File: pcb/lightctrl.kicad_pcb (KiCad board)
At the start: 2 copper layers, 71.1 x 22.9 mm, 30 parts, among them IC1 ESP-WROOM-02, P1 LED_CONN, P2 PROG, P3 IO, P4 BATT_SENSE, P5 5V, Q1 BSS138, Q2 IRF8788, SW1 SW_FLASH, SW2 SW_RST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

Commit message: Fixed bottom silkscreen text
Moved text away from pin headers
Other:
- board text added: "github.com/polygon/lightctrl"
- board text removed: "https://github.com/polygon/lightctrl"
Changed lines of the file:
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@@
     (links 73)
     (no_connects 0)
-    (area 77.419999 49.479999 148.640001 72.440001)
+    (area 71.511399 48.101 149.017334 73.886924)
     (thickness 1.6002)
     (drawings 34)
@@
   (page A4)
   (layers
-    (0 F.Cu signal)
-    (31 B.Cu signal)
+    (0 F.Cu signal hide)
+    (31 B.Cu signal hide)
     (36 B.SilkS user)
-    (37 F.SilkS user)
+    (37 F.SilkS user hide)
     (38 B.Mask user)
     (39 F.Mask user)
@@
     (effects (font (size 1 1) (thickness 0.15)))
   )
-  (gr_text https://github.com/polygon/lightctrl (at 78.1685 70.2945) (layer B.SilkS)
-    (effects (font (size 1.5 1.5) (thickness 0.3)) (justify right mirror))
-  )
-  (gr_text "Wi-Fi LED Controller\njan@legxaro.de\nchris@priseko.de" (at 147.32 67.945) (layer B.SilkS)
+  (gr_text github.com/polygon/lightctrl (at 78.232 67.056) (layer B.SilkS)
+    (effects (font (size 1.35 1.35) (thickness 0.3)) (justify right mirror))
+  )
+  (gr_text "Wi-Fi LED Controller\njan@legxaro.de\nchris@priseko.de" (at 144.399 64.77) (layer B.SilkS)
     (effects (font (size 1.5 1.5) (thickness 0.3)) (justify left mirror))
   )
-  (gr_text <<</>> (at 122.809 55.626) (layer B.SilkS)
-    (effects (font (size 7 7) (thickness 1.75)) (justify mirror))
+  (gr_text <<</>> (at 100.711 57.912) (layer B.SilkS)
+    (effects (font (size 6 6) (thickness 1.5)) (justify mirror))
   )
   (gr_text IO (at 108.458 67.564) (layer F.SilkS)

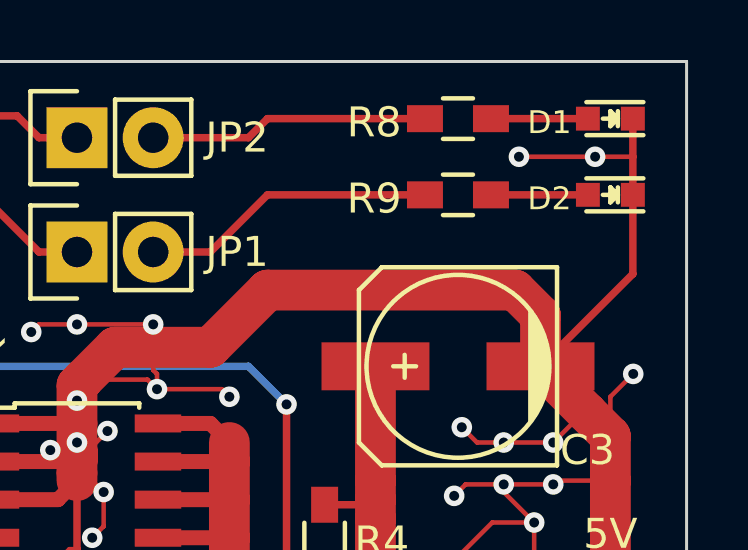
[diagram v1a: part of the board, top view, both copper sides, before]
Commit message: Replaced LED footprint with 3.2mmx1.6mm
Reasonable LED part available with that footprint
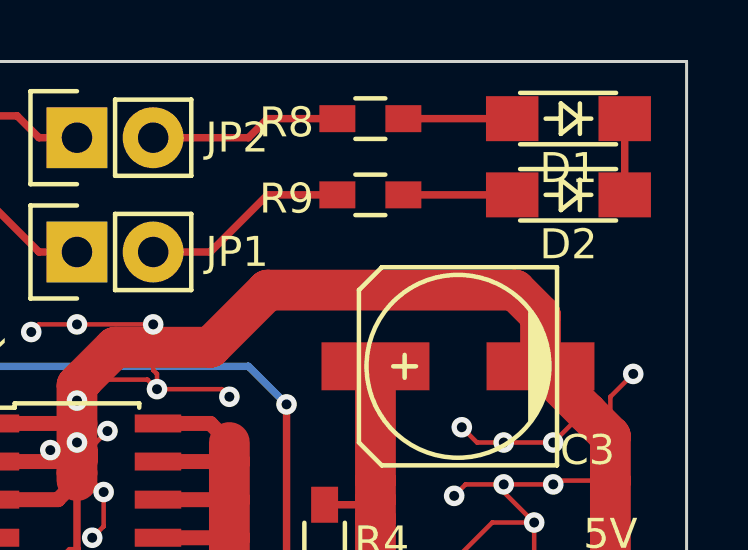
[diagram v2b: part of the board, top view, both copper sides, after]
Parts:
- D1, D2: footprint LEDs:LED_0603 -> leds:LED_3.2x1.6
- moved R8 2.92 mm to (138.0, 51.4)
- moved R9 2.92 mm to (138.0, 54.0)
- moved D1 1.40 mm to (144.7, 51.4)
- moved D2 1.40 mm to (144.7, 54.0)
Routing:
- net GND: track 123.7 -> 112.9 mm, vias 28 -> 26
- net Net-(JP2-Pad2): track 9.32 -> 6.40 mm
- net Net-(JP1-Pad2): track 9.85 -> 6.93 mm

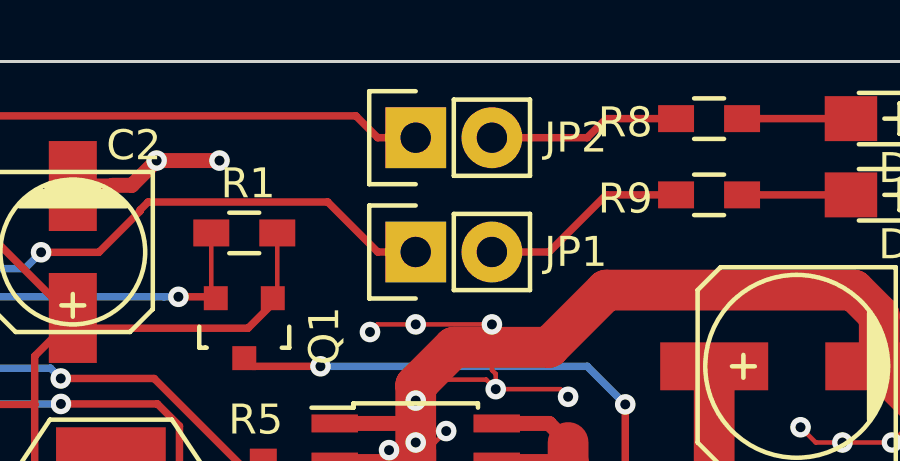
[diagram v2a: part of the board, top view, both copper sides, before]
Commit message: Routing and silkscreen fixes
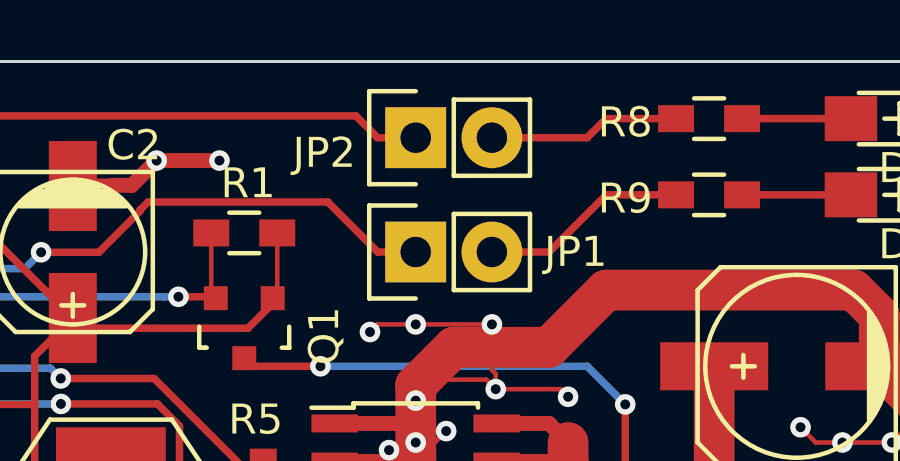
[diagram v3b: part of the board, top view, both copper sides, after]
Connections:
- IC1 pad 11: /ESP8266/RXI -> /ESP8266/TXO
- IC1 pad 12: /ESP8266/TXO -> /ESP8266/RXI
- P2 pad 2: /ESP8266/RXI -> /ESP8266/TXO
- P2 pad 3: /ESP8266/TXO -> /ESP8266/RXI
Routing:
- net /ESP8266/TXO: track 18.0 -> 20.2 mm
- net /ESP8266/RXI: track 20.2 -> 18.0 mm
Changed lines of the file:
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@@
   )
   (setup
-    (last_trace_width 0.25)
+    (last_trace_width 0.1524)
     (user_trace_width 0.25)
     (user_trace_width 0.5)
@@
       (net 13 /ESP8266/BOOT_SEL))
     (pad 11 smd oval (at 18 10.5 90) (size 2 0.9) (layers F.Cu F.Mask)
+      (net 15 /ESP8266/TXO))
+    (pad 12 smd oval (at 18 9 90) (size 2 0.9) (layers F.Cu F.Mask)
       (net 14 /ESP8266/RXI))
-    (pad 12 smd oval (at 18 9 90) (size 2 0.9) (layers F.Cu F.Mask)
-      (net 15 /ESP8266/TXO))
     (pad 13 smd oval (at 18 7.5 90) (size 2 0.9) (layers F.Cu F.Mask)
       (net 2 GND))
@@
     (descr "Through hole pin header")
     (tags "pin header")
-    (fp_text reference JP2 (at 0 5.334 180) (layer F.SilkS)
+    (fp_text reference JP2 (at -0.508 -3.048 180) (layer F.SilkS)
       (effects (font (size 1 1) (thickness 0.15)))
     )
@@
       (net 13 /ESP8266/BOOT_SEL))
     (pad 2 thru_hole oval (at 0 2.54 270) (size 2.032 1.7272) (drill 1.016) (layers *.Cu *.Mask F.SilkS)
+      (net 15 /ESP8266/TXO))
+    (pad 3 thru_hole oval (at 0 5.08 270) (size 2.032 1.7272) (drill 1.016) (layers *.Cu *.Mask F.SilkS)
       (net 14 /ESP8266/RXI))
-    (pad 3 thru_hole oval (at 0 5.08 270) (size 2.032 1.7272) (drill 1.016) (layers *.Cu *.Mask F.SilkS)
-      (net 15 /ESP8266/TXO))
     (pad 4 thru_hole oval (at 0 7.62 270) (size 2.032 1.7272) (drill 1.016) (layers *.Cu *.Mask F.SilkS)
       (net 1 +5V))
@@
   (segment (start 107.315 52.07) (end 107.315 56.72) (width 0.25) (layer F.Cu) (net 13))
   (segment (start 107.315 56.72) (end 105.075 58.96) (width 0.25) (layer F.Cu) (net 13))
-  (segment (start 89.965144 54.537789) (end 89.892933 54.61) (width 0.25) (layer B.Cu) (net 14))
-  (segment (start 104.648 53.848) (end 103.958211 54.537789) (width 0.25) (layer B.Cu) (net 14))
-  (segment (start 89.892933 54.61) (end 89.408 54.61) (width 0.25) (layer B.Cu) (net 14))
-  (segment (start 103.958211 54.537789) (end 89.965144 54.537789) (width 0.25) (layer B.Cu) (net 14))
-  (segment (start 89.408 54.61) (end 89.408 52.018) (width 0.25) (layer F.Cu) (net 14))
-  (segment (start 89.408 52.018) (end 89.24 51.85) (width 0.25) (layer F.Cu) (net 14))
-  (via (at 89.408 54.61) (size 0.6858) (drill 0.3302) (layers F.Cu B.Cu) (net 14))
-  (segment (start 104.775 52.07) (end 104.775 53.721) (width 0.25) (layer F.Cu) (net 14))
-  (segment (start 104.775 53.721) (end 104.648 53.848) (width 0.25) (layer F.Cu) (net 14))
-  (via (at 104.648 53.848) (size 0.6858) (drill 0.3302) (layers F.Cu B.Cu) (net 14))
-  (segment (start 87.884 53.848) (end 101.894294 53.848) (width 0.25) (layer B.Cu) (net 15))
-  (segment (start 101.894294 53.848) (end 102.10404 53.638254) (width 0.25) (layer B.Cu) (net 15))
-  (segment (start 102.235 53.507294) (end 102.10404 53.638254) (width 0.25) (layer F.Cu) (net 15))
-  (via (at 102.10404 53.638254) (size 0.6858) (drill 0.3302) (layers F.Cu B.Cu) (net 15))
-  (segment (start 102.235 52.07) (end 102.235 53.507294) (width 0.25) (layer F.Cu) (net 15))
-  (segment (start 87.74 53.704) (end 87.74 51.85) (width 0.25) (layer F.Cu) (net 15))
-  (segment (start 87.884 53.848) (end 87.74 53.704) (width 0.25) (layer F.Cu) (net 15))
-  (via (at 87.884 53.848) (size 0.6858) (drill 0.3302) (layers F.Cu B.Cu) (net 15))
+  (segment (start 87.884 53.848) (end 101.894294 53.848) (width 0.25) (layer B.Cu) (net 14))
+  (segment (start 101.894294 53.848) (end 102.10404 53.638254) (width 0.25) (layer B.Cu) (net 14))
+  (segment (start 102.235 53.507294) (end 102.10404 53.638254) (width 0.25) (layer F.Cu) (net 14))
+  (via (at 102.10404 53.638254) (size 0.6858) (drill 0.3302) (layers F.Cu B.Cu) (net 14))
+  (segment (start 102.235 52.07) (end 102.235 53.507294) (width 0.25) (layer F.Cu) (net 14))
+  (segment (start 87.74 53.704) (end 87.74 51.85) (width 0.25) (layer F.Cu) (net 14))
+  (segment (start 87.884 53.848) (end 87.74 53.704) (width 0.25) (layer F.Cu) (net 14))
+  (via (at 87.884 53.848) (size 0.6858) (drill 0.3302) (layers F.Cu B.Cu) (net 14))
+  (segment (start 89.965144 54.537789) (end 89.892933 54.61) (width 0.25) (layer B.Cu) (net 15))
+  (segment (start 104.648 53.848) (end 103.958211 54.537789) (width 0.25) (layer B.Cu) (net 15))
+  (segment (start 89.892933 54.61) (end 89.408 54.61) (width 0.25) (layer B.Cu) (net 15))
+  (segment (start 103.958211 54.537789) (end 89.965144 54.537789) (width 0.25) (layer B.Cu) (net 15))
+  (segment (start 89.408 54.61) (end 89.408 52.018) (width 0.25) (layer F.Cu) (net 15))
+  (segment (start 89.408 52.018) (end 89.24 51.85) (width 0.25) (layer F.Cu) (net 15))
+  (via (at 89.408 54.61) (size 0.6858) (drill 0.3302) (layers F.Cu B.Cu) (net 15))
+  (segment (start 104.775 52.07) (end 104.775 53.721) (width 0.25) (layer F.Cu) (net 15))
+  (segment (start 104.775 53.721) (end 104.648 53.848) (width 0.25) (layer F.Cu) (net 15))
+  (via (at 104.648 53.848) (size 0.6858) (drill 0.3302) (layers F.Cu B.Cu) (net 15))
   (segment (start 111.19612 56.02732) (end 110.109 54.9402) (width 0.25) (layer B.Cu) (net 16))
   (segment (start 110.109 54.9402) (end 90.37828 54.9402) (width 0.25) (layer B.Cu) (net 16))

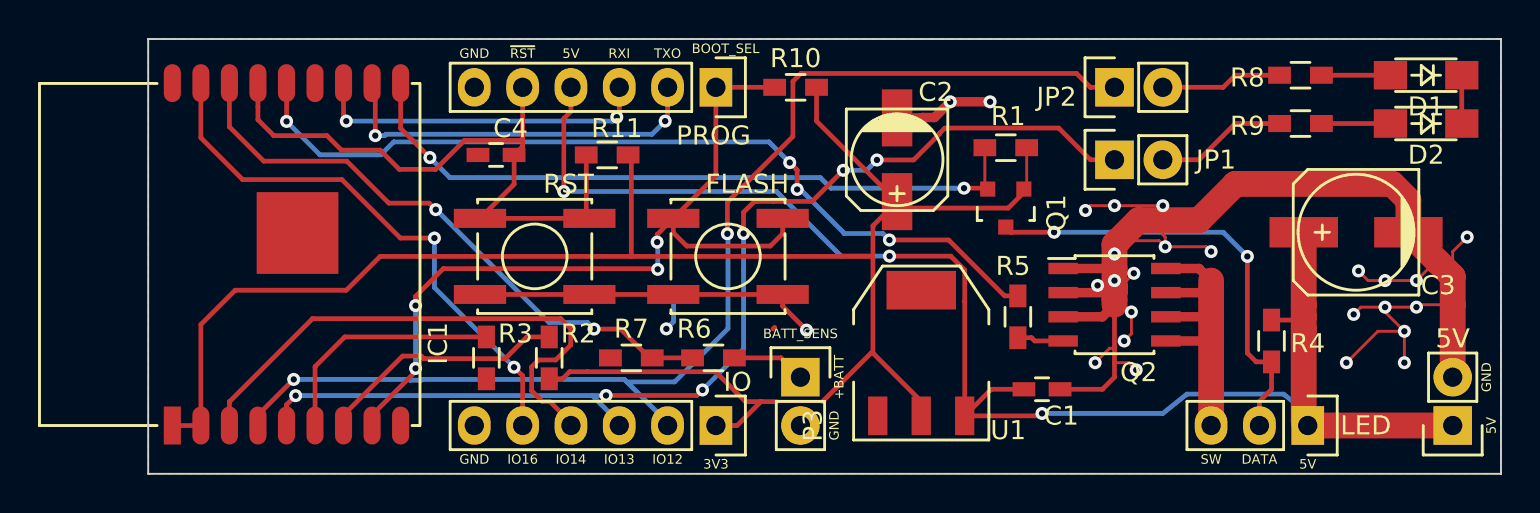
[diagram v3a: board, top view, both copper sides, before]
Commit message: Separated routing of data and +5V
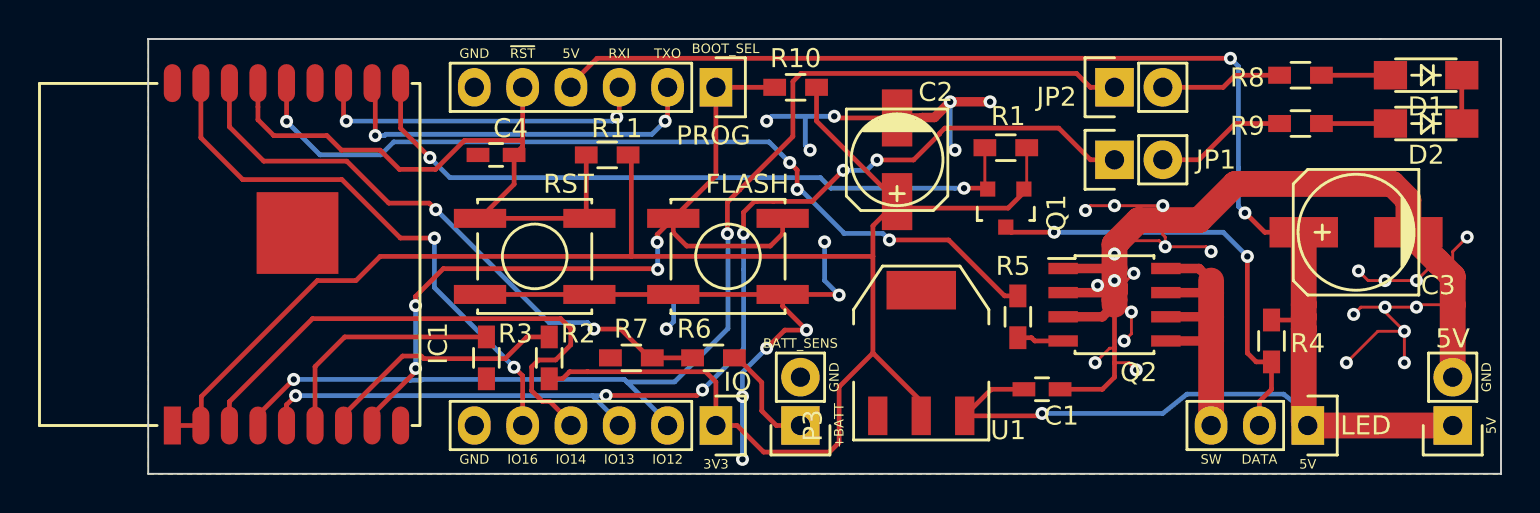
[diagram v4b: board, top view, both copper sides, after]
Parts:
- moved P4 2.54 mm to (111.8, 69.8), turned to 180 degrees
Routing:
- net GND: track 112.9 -> 139.4 mm, vias 26 -> 35
- net +5V: track 79.3 -> 90.6 mm
- net +BATT: track 3.89 -> 5.82 mm
- net +3V3: track 102.4 -> 101.6 mm

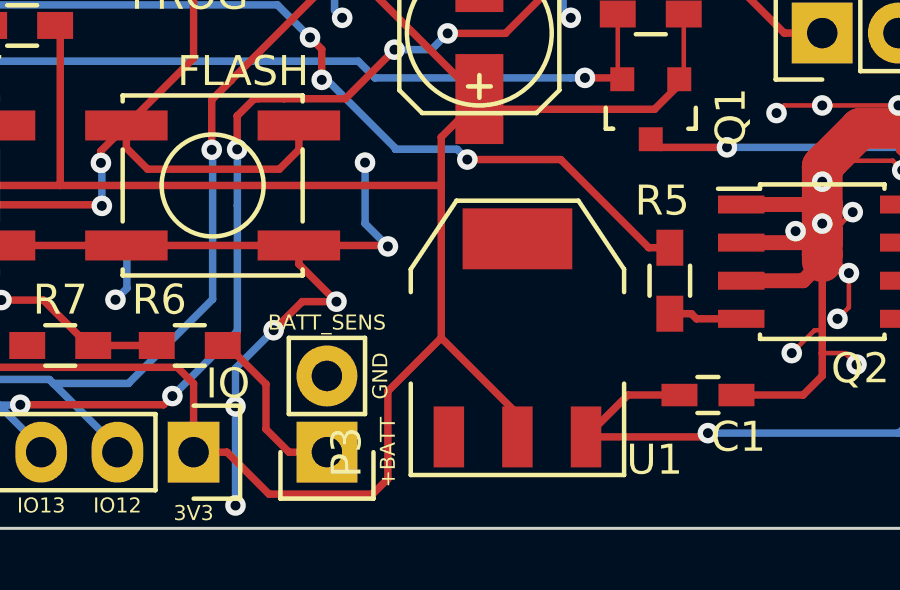
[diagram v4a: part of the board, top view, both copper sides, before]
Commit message: GND connection improvements
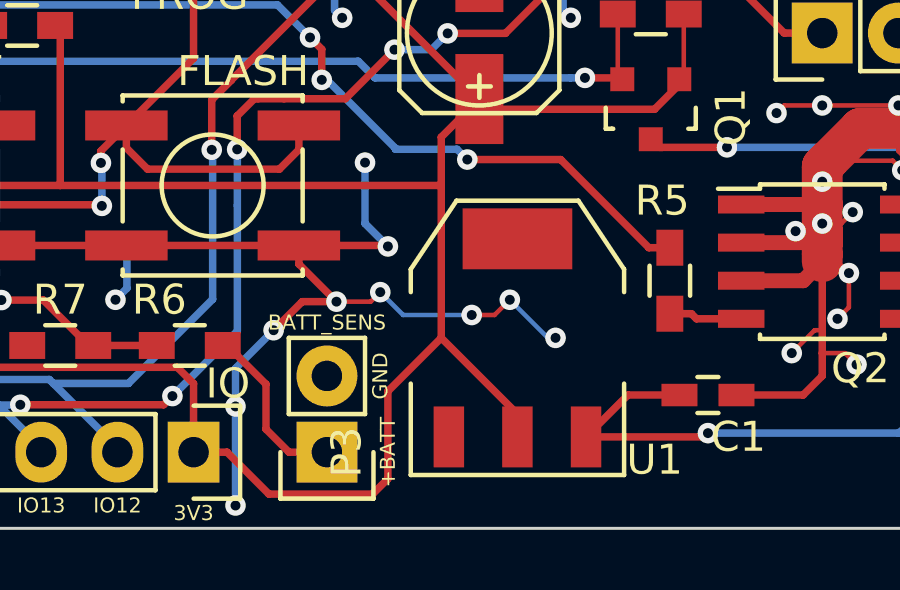
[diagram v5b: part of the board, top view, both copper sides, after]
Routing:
- net GND: track 139.4 -> 147.9 mm, vias 35 -> 39
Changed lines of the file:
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@@
   (general
     (links 73)
-    (no_connects 1)
-    (area 77.419999 49.479999 148.640001 72.440001)
+    (no_connects 0)
+    (area 71.511399 48.4526 148.640001 73.886924)
     (thickness 1.6002)
     (drawings 34)
-    (tracks 450)
+    (tracks 462)
     (zones 0)
     (modules 30)
@@
   )
   (setup
-    (last_trace_width 0.25)
+    (last_trace_width 0.1524)
     (user_trace_width 0.25)
     (user_trace_width 0.5)
@@
   (segment (start 138.21918 64.135) (end 138.21918 63.5) (width 1.36) (layer F.Cu) (net 1))
   (segment (start 138.21918 63.5) (end 138.21918 59.69) (width 1.36) (layer F.Cu) (net 1))
+  (segment (start 117.856 64.77) (end 119.126 66.04) (width 0.1524) (layer B.Cu) (net 2))
+  (via (at 119.38 66.04) (size 0.6858) (drill 0.3302) (layers F.Cu B.Cu) (net 2))
+  (segment (start 119.126 66.04) (end 119.38 66.04) (width 0.1524) (layer B.Cu) (net 2))
+  (segment (start 116.586 65.278) (end 117.348 65.278) (width 0.1524) (layer F.Cu) (net 2))
+  (via (at 117.856 64.77) (size 0.6858) (drill 0.3302) (layers F.Cu B.Cu) (net 2))
+  (segment (start 117.348 65.278) (end 117.856 64.77) (width 0.1524) (layer F.Cu) (net 2))
+  (segment (start 113.538 64.516) (end 114.3 65.278) (width 0.1524) (layer B.Cu) (net 2))
+  (segment (start 114.3 65.278) (end 116.586 65.278) (width 0.1524) (layer B.Cu) (net 2))
+  (via (at 116.586 65.278) (size 0.6858) (drill 0.3302) (layers F.Cu B.Cu) (net 2))
+  (segment (start 112.0775 64.8335) (end 113.2205 64.8335) (width 0.1524) (layer F.Cu) (net 2))
+  (segment (start 113.2205 64.8335) (end 113.538 64.516) (width 0.1524) (layer F.Cu) (net 2))
+  (via (at 113.538 64.516) (size 0.6858) (drill 0.3302) (layers F.Cu B.Cu) (net 2))
   (segment (start 119.634 52.832) (end 119.634 55.118) (width 0.25) (layer B.Cu) (net 2))
   (segment (start 119.634 55.118) (end 119.888 55.372) (width 0.25) (layer B.Cu) (net 2))
